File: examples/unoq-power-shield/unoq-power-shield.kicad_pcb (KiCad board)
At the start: 4 copper layers, 53.3 x 68.6 mm, 56 parts, among them J1 VIN 7-24V, J10 UNO PWR, J11 UNO ANALOG, J12 UNO D0-D7, J13 UNO D8-SCL, J2 5V OUT, J3 Qwiic, J4 Qwiic, J5 5V IO, Q1 BSS138LT1G, Q2 BSS138LT1G, Q3 BSS138LT1G, Q4 BSS138LT1G, Q5 AO4407A, U1 TPS54331DDAR, U2 INA226AIDGSR

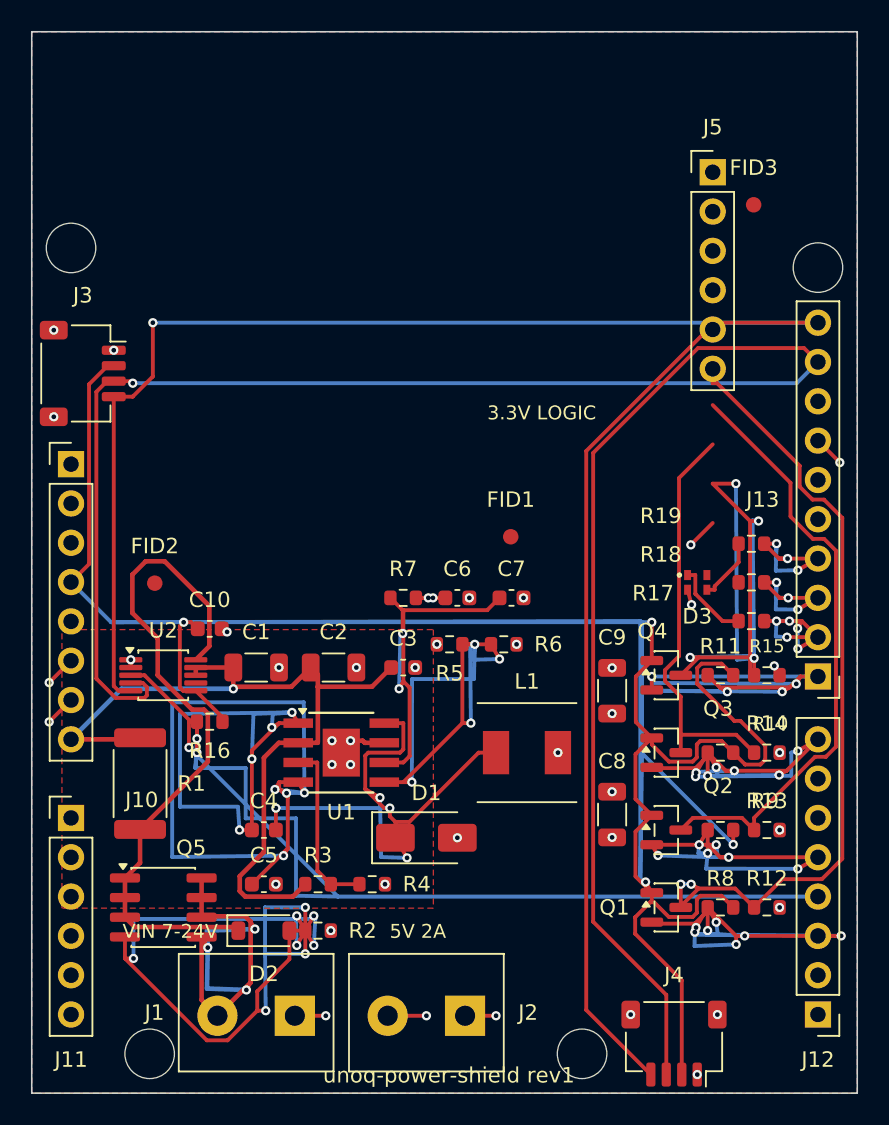
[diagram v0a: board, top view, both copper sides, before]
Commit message: Example board: gerber checker green (14/0); idempotency proven byte-for-byte
Round 4: J5 moved off D3 (its pins run DOWNWARD from pin1 - pin 6 landed
on the LED and shorted RGB_G to GND), netclass clearance aligned to
KiCad's 0.2 DRC default end to end (freerouting was routing to the
bootstrapped 0.15 and every squeeze became a DRC violation), a real
VIN_RAW pour over the 4 A entry corridor, GND stitching vias on the
Qwiic mounting tabs.

The checker now passes the board's own export: 14 passed / 2 not checked
/ 0 failed, with plane_fed exempting exactly the 9 measured pad-escape
stubs (15.6 mm, all chains <= 3 mm). Run-twice-diff idempotency:
generate_schematic, floorplan and add_mounting_holes are byte-identical
on the second run.

Still open before this board is orderable (the plan's gate list holds
it): 9 clearance squeezes in the buck cluster (completion passes use
their own 0.16 defaults - set [route.completion] clearance next), a 2 mm
5V hop at D3, one GND island wanting a stitch. DRC is stable across all
5 samples; no unstable kinds.

Co-Authored-By: Claude Fable 5 <noreply@anthropic.com>
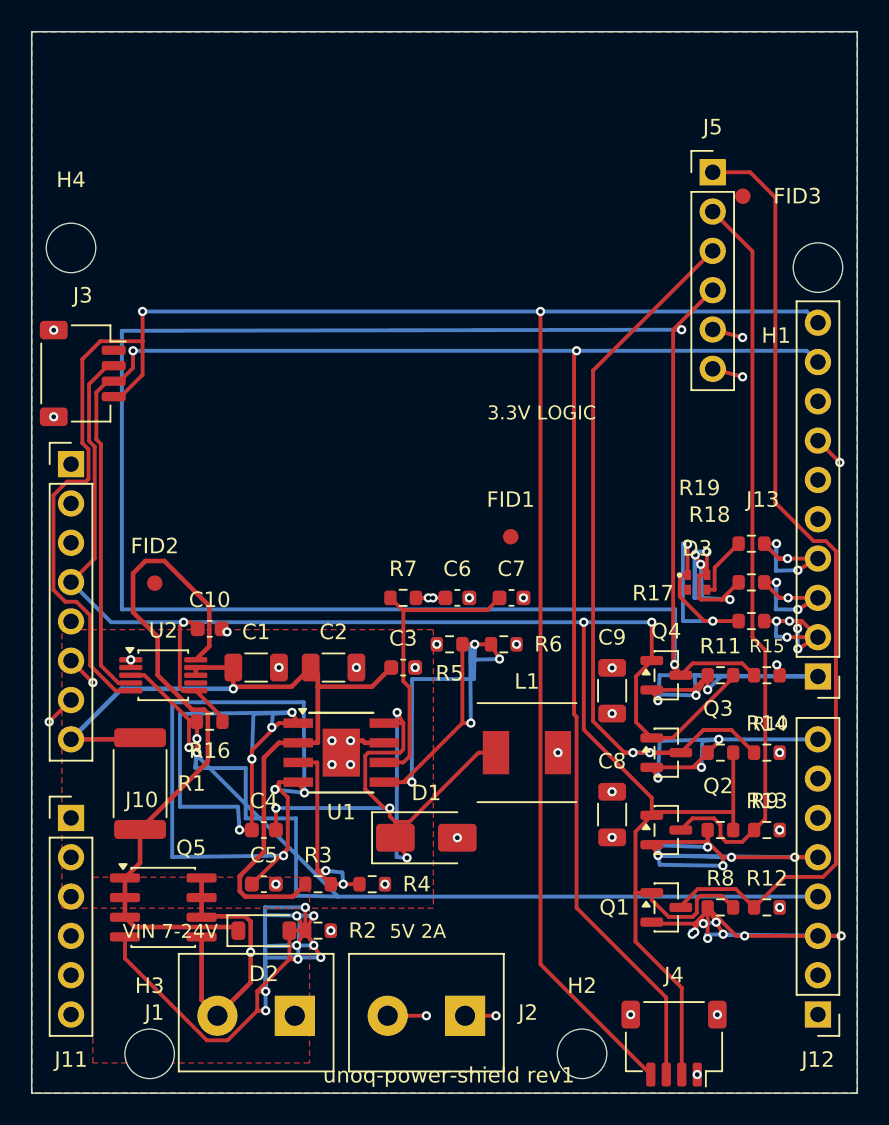
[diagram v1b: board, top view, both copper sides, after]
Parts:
- moved FID3 0.89 mm to (167.8, 81.3)
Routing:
- net HV4: track 48.1 -> 126.4 mm, vias 4 -> 2
- net 3V3_UNO: track 202.6 -> 130.5 mm, vias 4 -> 3
- net HV3: track 26.8 -> 49.7 mm, vias 0 -> 2
- net RGB_G: track 0.00 -> 20.4 mm, vias 0 -> 4
- net LV3: track 36.3 -> 21.9 mm, vias 7 -> 3
- net SDA_3V3: track 131.4 -> 118.2 mm, vias 1 -> 2
- net LV4: track 44.9 -> 32.4 mm, vias 4 -> 3
- net VIN_RAW: track 29.6 -> 18.3 mm, vias 3 -> 1
- net RGB_R: track 5.24 -> 16.1 mm, vias 0 -> 2
- net HV1: track 51.4 -> 62.1 mm, vias 2 -> 0
- net HV2: track 39.2 -> 48.1 mm
- net LV2: track 30.8 -> 38.5 mm, vias 6 -> 5
- net COMP: track 24.9 -> 19.1 mm, vias 2 -> 0
- net PH: track 37.1 -> 41.3 mm
- net LV1: track 37.9 -> 34.1 mm, vias 7 -> 8
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- added copper zone on F.Cu, net VIN_RAW
